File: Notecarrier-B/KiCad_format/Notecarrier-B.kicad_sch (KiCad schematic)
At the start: 62 parts, among them J19 MICROUSB-B, J20 MDT420E01001, J21 NU, J22 NU, J23 S2B-PH-SM4-TB(LF)(SN), J24 SM04B-SRSS-TBT, Q2 AO3420, U3 MAX17225ELT, U4 TPS62748YFPT, U5 MCP73831-2ACI/MC

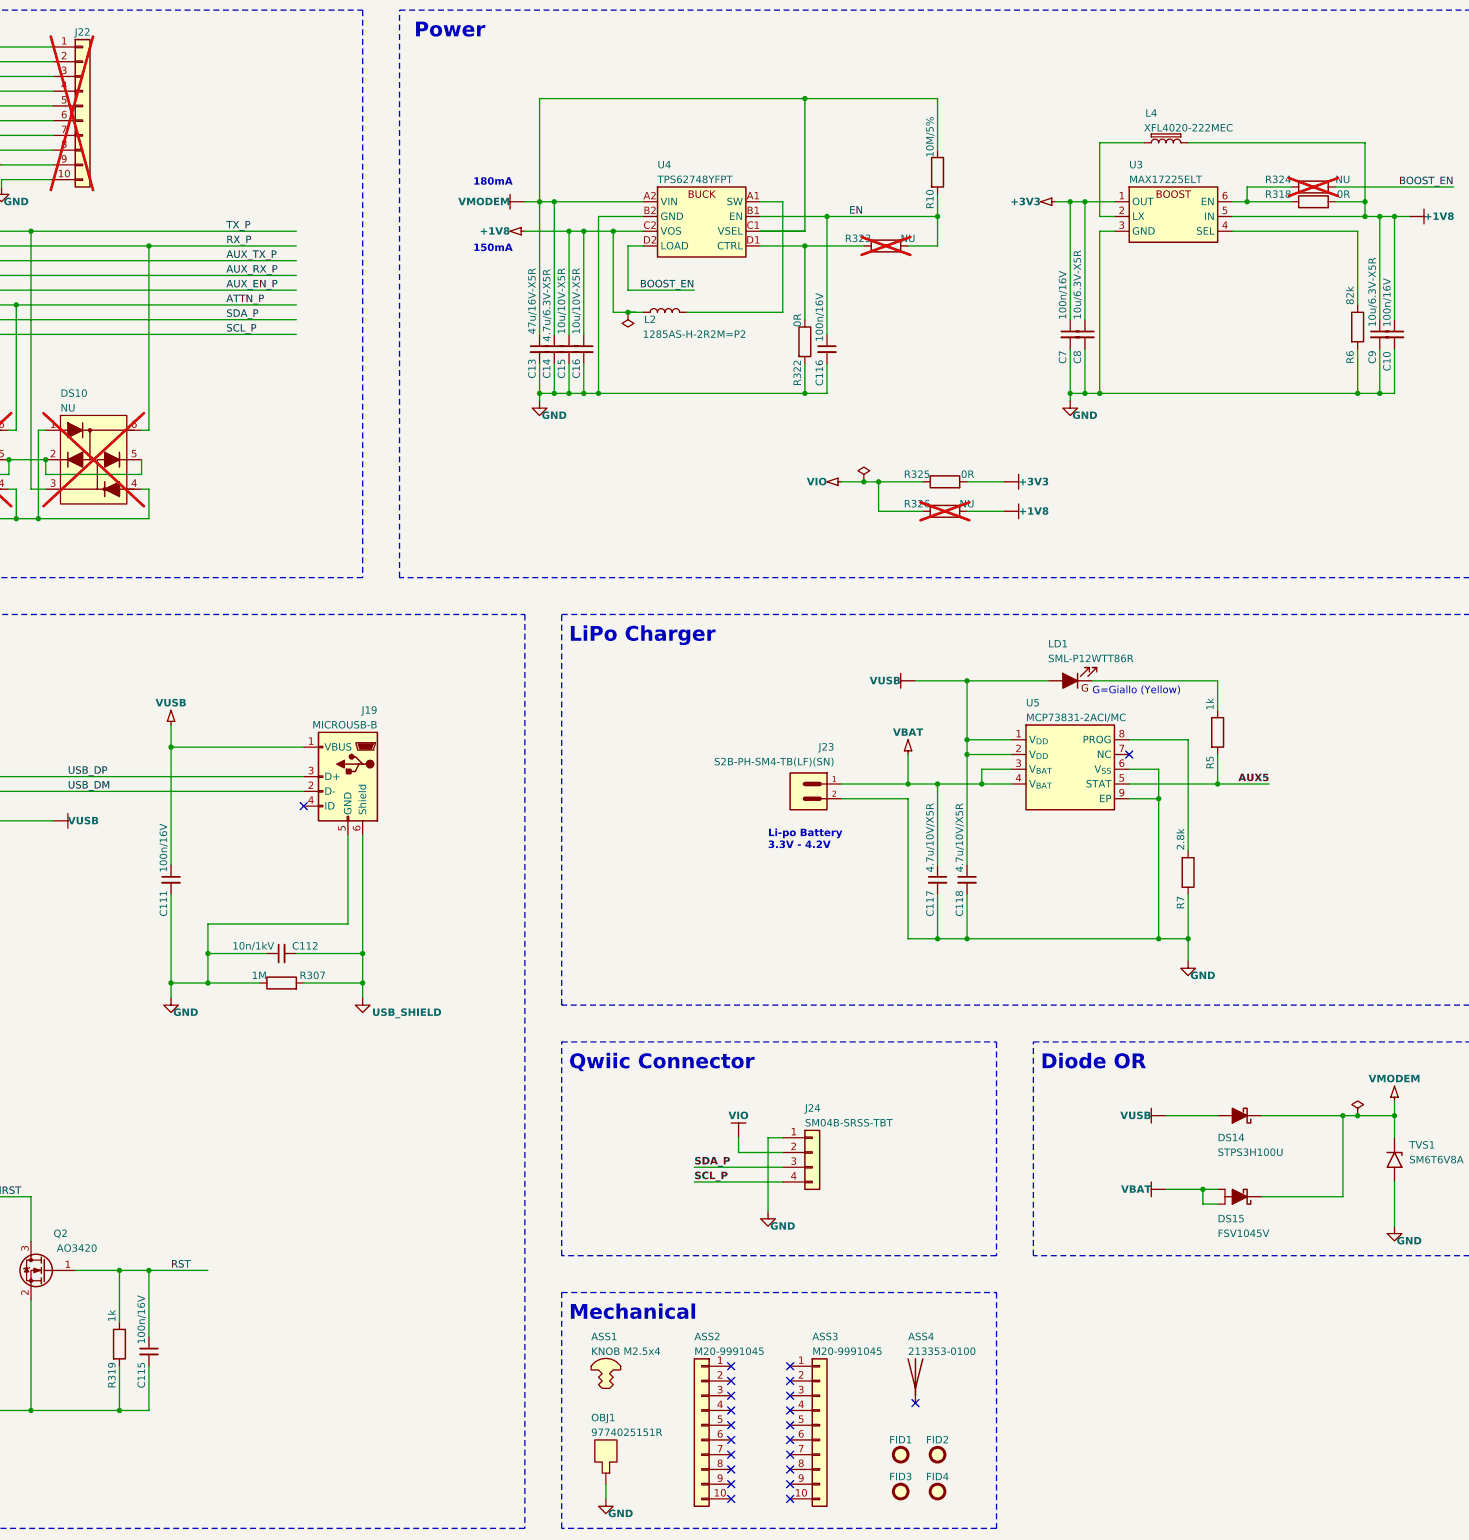
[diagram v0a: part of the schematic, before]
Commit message: Port PCB and do validation for Notecarrier-B
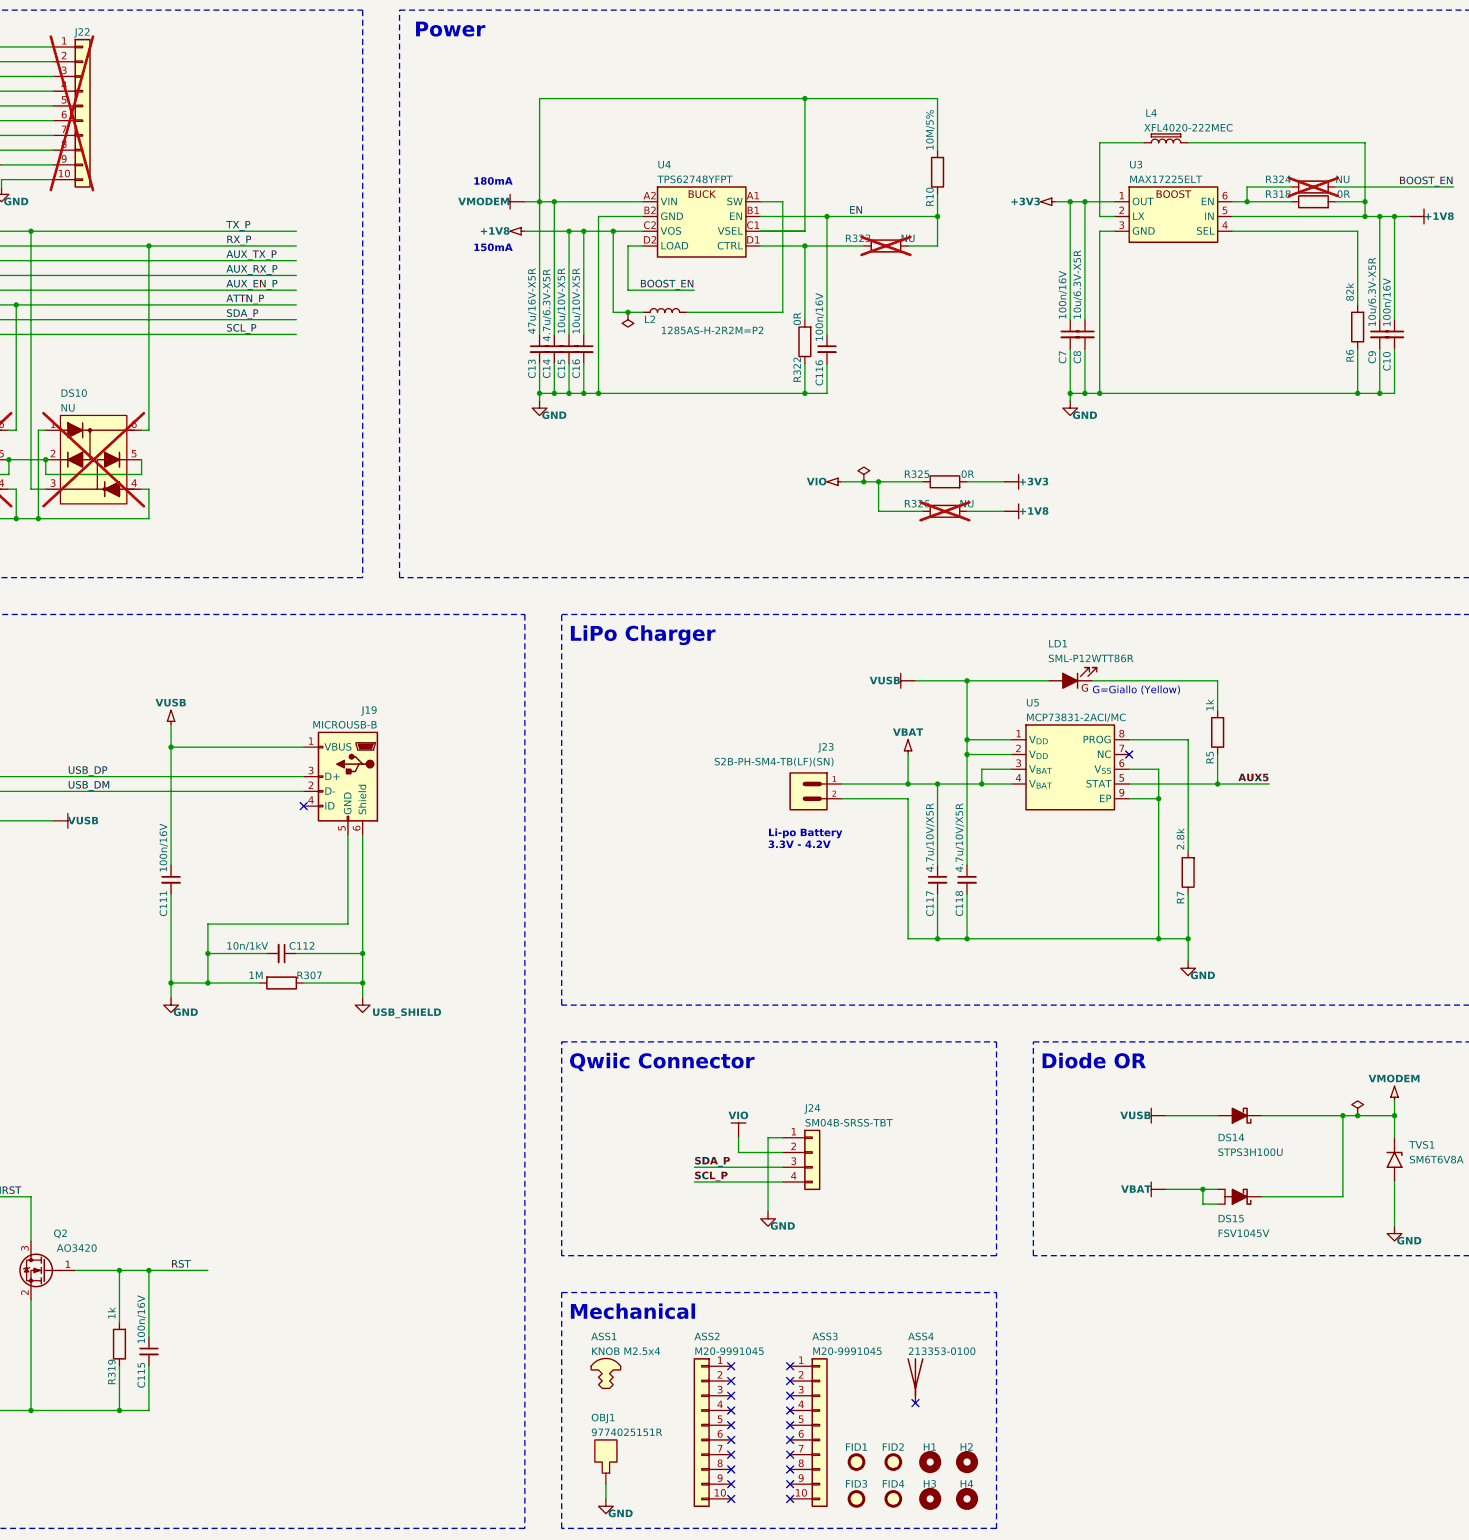
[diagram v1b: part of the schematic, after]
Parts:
- added H1, H2, H3, H4: MountingHole, Notecarrier-B:FORO-0330-U, symbol Mechanical:MountingHole
- C10, C111, C115, C116, C14, C7, C8, C9: footprint Capacitor_SMD:C_0402_1005Metric -> Notecarrier-B:CS-C-0402
- C112, C13: footprint Capacitor_SMD:C_1206_3216Metric -> Notecarrier-B:CS-C-1206
- C113: footprint (none) -> Notecarrier-B:CS-T-A
- C114: footprint (none) -> Notecarrier-B:CS-T-B
- C117, C118, C15, C16: footprint Capacitor_SMD:C_0603_1608Metric -> Notecarrier-B:CS-C-0603
- DS10, DS4, DS5, DS6: footprint Package_TO_SOT_SMD:SOT-563 -> Notecarrier-B:SOT563
- DS14, TVS1: footprint Diode_SMD:D_SMB -> Notecarrier-B:SMB
- DS15: footprint Package_TO_SOT_SMD:TO-277A -> Notecarrier-B:TO277-3
- DSW1: footprint (none) -> Notecarrier-B:DSS-CHS-01TB
- F1, F2: footprint Fuse:Fuse_0603_1608Metric -> Notecarrier-B:FS-0603
- FID1, FID2, FID3, FID4: footprint (none) -> Notecarrier-B:FIDUCIAL
- J19: footprint (none) -> Notecarrier-B:J-5-0065-FOS-MICROUSB10118192
- J20: footprint blues-kicad-lib:MDT420E01001 -> Notecarrier-B:J-75-0050-MOS-M2-E
- J21, J22: footprint (none) -> Notecarrier-B:J-10-0254-MDT
- J23: footprint blues-kicad-lib:JST_S2B-PH-SM4-TB(LF)(SN) -> Notecarrier-B:J-2-0200-MOS-S2B
- J24: footprint (none) -> Notecarrier-B:J-4-0100-MOS-SH
- L2: footprint Inductor_SMD:L_0805_2012Metric -> Notecarrier-B:LS-0806
- L4: footprint Inductor_SMD:L_Coilcraft_XxL4020 -> Notecarrier-B:LS-XFL4020
- LD1: footprint (none) -> Notecarrier-B:LD-0402
- OBJ1: footprint (none) -> Notecarrier-B:DIST-WASMSIM0250
- Q2: footprint Package_TO_SOT_SMD:SOT-23 -> Notecarrier-B:SOT23
- R10, R318, R319, R322, R325, R6: footprint Resistor_SMD:R_0402_1005Metric -> Notecarrier-B:RS-0402
- R307: footprint Resistor_SMD:R_1206_3216Metric -> Notecarrier-B:RS-1206
- R323, R324, R326: footprint (none) -> Notecarrier-B:RS-0402
- R5, R7: footprint Resistor_SMD:R_0201_0603Metric -> Notecarrier-B:RS-0201
- RR1, RR2: footprint (none) -> Notecarrier-B:RR-8X-1506
- U3: footprint (none) -> Notecarrier-B:WDFN6-0200X0200
- U4: footprint Package_BGA:Texas_DSBGA-8_0.705x1.468mm_Layout2x4_P0.4mm -> Notecarrier-B:XFBGA8
- U5: footprint Package_DFN_QFN:DFN-8-1EP_3x2mm_P0.5mm_EP1.75x1.45mm -> Notecarrier-B:VFDFN8-EXP
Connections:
- net +1V8: now also L2.2; no longer L2.1
- net AUX5: now also R5.1; no longer R5.2
- net EN: now also R10.1; no longer R10.2
- net GND: now also C112.2, R307.2, R319.1, R322.1, R6.1, R7.1; no longer C112.1, R307.1, R319.2, R322.2, R6.2, R7.2
- net RST: now also R319.2; no longer R319.1
- net VMODEM: now also R10.2; no longer R10.1
- net at U4.A1 (SW): now also L2.1; no longer L2.2
- net at R323.1, U4.D1 (CTRL): now also R322.2; no longer R322.1
- net at U3.4 (SEL): now also R6.2; no longer R6.1
- net at LD1.1 (K): now also R5.2; no longer R5.1
- net at U5.8 (PROG): now also R7.2; no longer R7.1
- new net: C112.1, J19.6 (Shield), R307.1
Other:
- moved on the sheet: C112, FID1, FID2, FID3, FID4, L2, R10, R307, R319, R322, R5, R6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

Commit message: Move all Notecarrier-B parts into blues-kicad-lib
- all symbols, footprints and 3d-models which lived in the Notecarrier-B project consolidated into the blues-kicad-lib library.
- the BLUES_KICAD_LIB_DIR environment variable created and all links updated.
- PortingNotes.md updated with the rationale and method
- README.md updated with a reference to the library in accordance with the rationale in PortingNotes.
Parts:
- ASS1: symbol Notecarrier-B:mechanical_Screw -> blues-kicad-lib:mechanical_Screw
- C10, C111, C115, C116, C14, C7, C8, C9: footprint Notecarrier-B:CS-C-0402 -> blues-kicad-lib:CS-C-0402
- C112, C13: footprint Notecarrier-B:CS-C-1206 -> blues-kicad-lib:CS-C-1206
- C113: footprint Notecarrier-B:CS-T-A -> blues-kicad-lib:CS-T-A
- C114: footprint Notecarrier-B:CS-T-B -> blues-kicad-lib:CS-T-B
- C117, C118, C15, C16: footprint Notecarrier-B:CS-C-0603 -> blues-kicad-lib:CS-C-0603
- DS10, DS4, DS5, DS6: footprint Notecarrier-B:SOT563 -> blues-kicad-lib:SOT563; symbol Notecarrier-B:BAV99BRVA -> blues-kicad-lib:BAV99BRVA
- DS14, TVS1: footprint Notecarrier-B:SMB -> blues-kicad-lib:SMB
- DS15: footprint Notecarrier-B:TO277-3 -> blues-kicad-lib:TO277-3; symbol Notecarrier-B:FSV1045V -> blues-kicad-lib:FSV1045V
- DSW1: footprint Notecarrier-B:DSS-CHS-01TB -> blues-kicad-lib:DSS-CHS-01TB
- F1, F2: footprint Notecarrier-B:FS-0603 -> blues-kicad-lib:FS-0603
- FID1, FID2, FID3, FID4: footprint Notecarrier-B:FIDUCIAL -> blues-kicad-lib:FIDUCIAL
- H1, H2, H3, H4: footprint Notecarrier-B:FORO-0330-U -> blues-kicad-lib:FORO-0330-U
- J19: footprint Notecarrier-B:J-5-0065-FOS-MICROUSB10118192 -> blues-kicad-lib:J-5-0065-FOS-MICROUSB10118192
- J20: footprint Notecarrier-B:J-75-0050-MOS-M2-E -> blues-kicad-lib:J-75-0050-MOS-M2-E; symbol Notecarrier-B:MDT420E01001 -> blues-kicad-lib:MDT420E01001
- J21, J22: footprint Notecarrier-B:J-10-0254-MDT -> blues-kicad-lib:J-10-0254-MDT
- J23: footprint Notecarrier-B:J-2-0200-MOS-S2B -> blues-kicad-lib:J-2-0200-MOS-S2B; symbol Notecarrier-B:S2B-PH-SM4-TB(LF)(SN) -> blues-kicad-lib:S2B-PH-SM4-TB(LF)(SN)
- J24: footprint Notecarrier-B:J-4-0100-MOS-SH -> blues-kicad-lib:J-4-0100-MOS-SH
- L2: footprint Notecarrier-B:LS-0806 -> blues-kicad-lib:LS-0806
- L4: footprint Notecarrier-B:LS-XFL4020 -> blues-kicad-lib:LS-XFL4020; symbol Notecarrier-B:L_Shielded -> blues-kicad-lib:L_Shielded
- LD1: footprint Notecarrier-B:LD-0402 -> blues-kicad-lib:LD-0402; symbol Notecarrier-B:LED_Filled_Yellow -> blues-kicad-lib:LED_Filled_Yellow
- OBJ1: footprint Notecarrier-B:DIST-WASMSIM0250 -> blues-kicad-lib:DIST-WASMSIM0250; symbol Notecarrier-B:mechanical_Standoff_Pad -> blues-kicad-lib:mechanical_Standoff_Pad
- Q2: footprint Notecarrier-B:SOT23 -> blues-kicad-lib:SOT23; symbol Notecarrier-B:AO3420 -> blues-kicad-lib:AO3420
- R10, R318, R319, R322, R323, R324, R325, R326, R6: footprint Notecarrier-B:RS-0402 -> blues-kicad-lib:RS-0402
- R307: footprint Notecarrier-B:RS-1206 -> blues-kicad-lib:RS-1206
- R5, R7: footprint Notecarrier-B:RS-0201 -> blues-kicad-lib:RS-0201
- RR1, RR2: footprint Notecarrier-B:RR-8X-1506 -> blues-kicad-lib:RR-8X-1506
- U3: footprint Notecarrier-B:WDFN6-0200X0200 -> blues-kicad-lib:WDFN6-0200X0200; symbol Notecarrier-B:MAX17225ELT -> blues-kicad-lib:MAX17225ELT
- U4: footprint Notecarrier-B:XFBGA8 -> blues-kicad-lib:XFBGA8; symbol Notecarrier-B:TPS62748 -> blues-kicad-lib:TPS62748
- U5: footprint Notecarrier-B:VFDFN8-EXP -> blues-kicad-lib:VFDFN8-EXP; symbol Notecarrier-B:MCP73831-2ACI/MC -> blues-kicad-lib:MCP73831-2ACI/MC

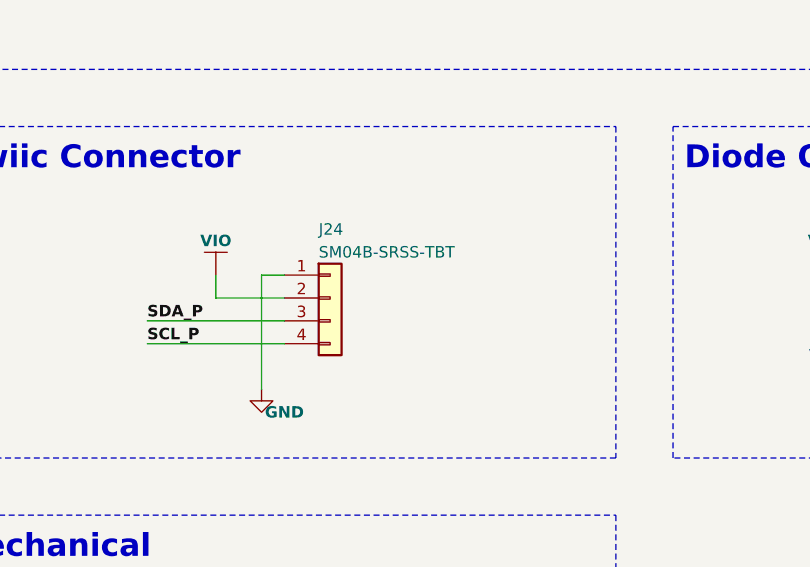
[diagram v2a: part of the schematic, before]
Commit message: Back fill symbol for SM04B-SRSS-TB / BM04B-SRSS-TBT.
Symbol created in the process of porting Notecarrier-A. Creating the symbol wasn’t justified when porting -B and -F, now it exists it’s best to be consistent even though these are SM04B-SRSS-TB (side entry) and the symbol was created for BM04B-SRSS-TBT (top entry).
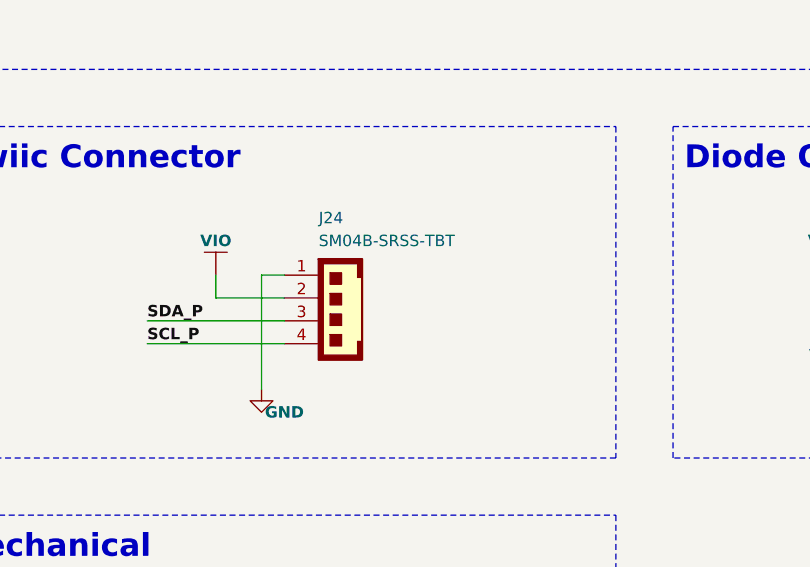
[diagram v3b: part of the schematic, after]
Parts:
- J24: symbol Connector_Generic:Conn_01x04 -> blues-kicad-lib:BM04B-SRSS-TBT
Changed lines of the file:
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@@
     )
   )
-  (symbol (lib_id "Connector_Generic:Conn_01x04") (at 278.13 214.63 0) (unit 1)
+  (symbol (lib_id "blues-kicad-lib:BM04B-SRSS-TBT") (at 278.13 214.63 0) (unit 1)
     (in_bom yes) (on_board yes) (dnp no)
-    (property "Reference" "J24" (at 276.86 207.01 0)
+    (property "Reference" "J24" (at 276.86 205.74 0)
       (effects (font (size 1.27 1.27)) (justify left))
     )
-    (property "Value" "SM04B-SRSS-TBT" (at 276.86 209.55 0)
+    (property "Value" "SM04B-SRSS-TBT" (at 276.86 208.28 0)
       (effects (font (size 1.27 1.27)) (justify left))
     )
@@
       (effects (font (size 1.27 1.27)) hide)
     )
+    (property "Critical" "" (at 278.13 214.63 0)
+      (effects (font (size 1.27 1.27)) hide)
+    )
+    (property "Manufacturer" "" (at 278.13 214.63 0)
+      (effects (font (size 1.27 1.27)) hide)
+    )
+    (property "Order Code" "" (at 278.13 214.63 0)
+      (effects (font (size 1.27 1.27)) hide)
+    )
+    (property "Part Number" "" (at 278.13 214.63 0)
+      (effects (font (size 1.27 1.27)) hide)
+    )
+    (property "Supplier" "" (at 278.13 214.63 0)
+      (effects (font (size 1.27 1.27)) hide)
+    )
